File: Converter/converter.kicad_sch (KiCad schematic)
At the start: 30 parts, among them IC1 NCP5109ADR2G, IC2 NCP5109ADR2G

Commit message: assigned footprints for some passives
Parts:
- R_{small,bottom}1, R_{small,bottom}2, R_{small,top}1, R_{small,top}2: value R_small -> 0.75; footprint (none) -> Resistor_SMD:R_0603_1608Metric_Pad0.98x0.95mm_HandSolder
- TP1, TP2, TP3, TP4, TP5, TP6: footprint (none) -> TestPoint:TestPoint_Bridge_Pitch2.0mm_Drill0.7mm
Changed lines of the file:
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@@
 			)
 		)
-		(property "Footprint" ""
+		(property "Footprint" "TestPoint:TestPoint_Bridge_Pitch2.0mm_Drill0.7mm"
 			(at 147.32 118.11 0)
 			(effects
@@
 			)
 		)
-		(property "Value" "R_small"
+		(property "Value" "0.75"
 			(at 96.52 108.712 90)
 			(effects
@@
 			)
 		)
-		(property "Footprint" ""
+		(property "Footprint" "Resistor_SMD:R_0603_1608Metric_Pad0.98x0.95mm_HandSolder"
 			(at 96.774 105.664 90)
 			(effects
@@
 			)
 		)
-		(property "Value" "R_small"
+		(property "Value" "0.75"
 			(at 96.52 140.208 90)
 			(effects
@@
 			)
 		)
-		(property "Footprint" ""
+		(property "Footprint" "Resistor_SMD:R_0603_1608Metric_Pad0.98x0.95mm_HandSolder"
 			(at 96.774 136.144 90)
 			(effects
@@
 			)
 		)
-		(property "Value" "R_small"
+		(property "Value" "0.75"
 			(at 96.52 150.114 90)
 			(effects
@@
 			)
 		)
-		(property "Footprint" ""
+		(property "Footprint" "Resistor_SMD:R_0603_1608Metric_Pad0.98x0.95mm_HandSolder"
 			(at 96.774 146.304 90)
 			(effects
@@
 			)
 		)
-		(property "Footprint" ""
+		(property "Footprint" "TestPoint:TestPoint_Bridge_Pitch2.0mm_Drill0.7mm"
 			(at 172.72 118.11 0)
 			(effects
@@
 			)
 		)
-		(property "Footprint" ""
+		(property "Footprint" "TestPoint:TestPoint_Bridge_Pitch2.0mm_Drill0.7mm"
 			(at 147.32 107.95 0)
 			(effects
@@
 			)
 		)
-		(property "Footprint" ""
+		(property "Footprint" "TestPoint:TestPoint_Bridge_Pitch2.0mm_Drill0.7mm"
 			(at 172.72 107.95 0)
 			(effects
@@
 			)
 		)
-		(property "Value" "R_small"
+		(property "Value" "0.75"
 			(at 96.52 119.126 90)
 			(effects
@@
 			)
 		)
-		(property "Footprint" ""
+		(property "Footprint" "Resistor_SMD:R_0603_1608Metric_Pad0.98x0.95mm_HandSolder"
 			(at 96.774 115.824 90)
 			(effects
@@
 			)
 		)
-		(property "Footprint" ""
+		(property "Footprint" "TestPoint:TestPoint_Bridge_Pitch2.0mm_Drill0.7mm"
 			(at 172.72 97.79 0)
 			(effects
@@
 			)
 		)
-		(property "Footprint" ""
+		(property "Footprint" "TestPoint:TestPoint_Bridge_Pitch2.0mm_Drill0.7mm"
 			(at 147.32 97.79 0)
 			(effects

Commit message: more simulation work + fixed some things in root schematic
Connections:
- net +10V renamed +12V
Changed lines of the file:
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@@
 		)
 	)
-	(hierarchical_label "+10V"
+	(hierarchical_label "+12V"
 		(shape input)
 		(at 34.29 97.79 180)
@@
 		)
 	)
-	(hierarchical_label "+10V"
+	(hierarchical_label "+12V"
 		(shape input)
 		(at 34.29 128.27 180)

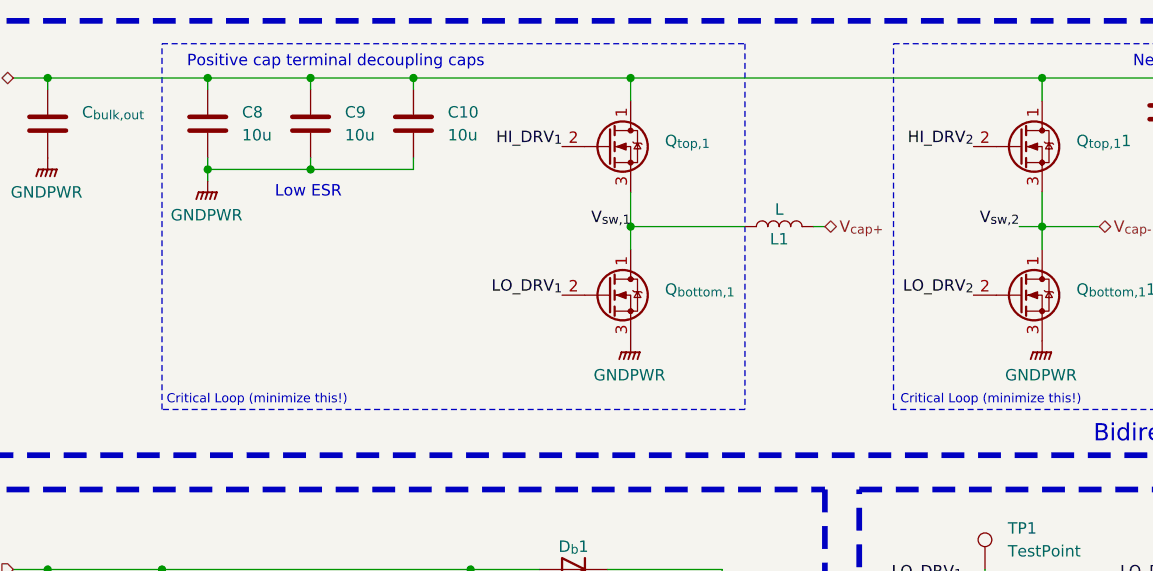
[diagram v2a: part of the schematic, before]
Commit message: fixed inductor connection
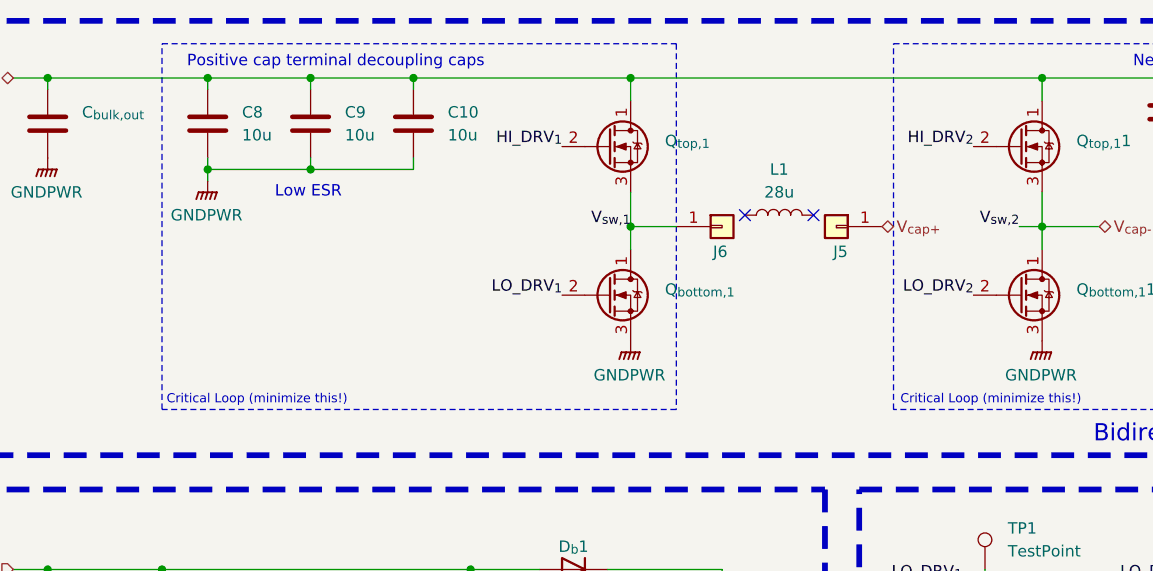
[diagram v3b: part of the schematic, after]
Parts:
- added J5, J6: Conn_01x01, NCP5109ADR2G:Inductor_wire_conn, symbol Connector_Generic:Conn_01x01
- L1: value L -> 28u
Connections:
- net V_{cap+}: now also J5.1 (Pin_1); no longer L1.2
- net V_{sw,1}: now also J6.1 (Pin_1); no longer L1.1
- no-connect marks 0 -> 2
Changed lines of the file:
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@@
 	(rectangle
 		(start 50.8 39.37)
-		(end 115.57 80.01)
+		(end 107.95 80.01)
 		(stroke
 			(width 0)
@@
 		(color 0 0 0 0)
 	)
+	(no_connect
+		(at 123.19 58.42)
+	)
+	(no_connect
+		(at 115.57 58.42)
+	)
 	(wire
 		(pts
@@
 	(wire
 		(pts
-			(xy 102.87 59.69) (xy 102.87 62.23)
-		)
-		(stroke
-			(width 0)
-			(type default)
-		)
-	)
-	(wire
-		(pts
 			(xy 85.09 106.68) (xy 85.09 97.79)
 		)
@@
 	(wire
 		(pts
+			(xy 102.87 59.69) (xy 107.95 59.69)
+		)
+		(stroke
+			(width 0)
+			(type default)
+		)
+	)
+	(wire
+		(pts
 			(xy 167.64 107.95) (xy 167.64 109.22)
 		)
@@
 	(wire
 		(pts
-			(xy 123.19 59.69) (xy 124.46 59.69)
+			(xy 55.88 43.18) (xy 67.31 43.18)
 		)
 		(stroke
@@
 	(wire
 		(pts
-			(xy 55.88 43.18) (xy 67.31 43.18)
+			(xy 162.56 52.07) (xy 173.99 52.07)
 		)
 		(stroke
@@
 	(wire
 		(pts
-			(xy 162.56 52.07) (xy 173.99 52.07)
+			(xy 102.87 59.69) (xy 102.87 62.23)
 		)
 		(stroke
@@
 	(wire
 		(pts
-			(xy 102.87 59.69) (xy 115.57 59.69)
-		)
-		(stroke
-			(width 0)
-			(type default)
-		)
-	)
-	(wire
-		(pts
 			(xy 173.99 43.18) (xy 185.42 43.18)
 		)
@@
 	(hierarchical_label "V_{cap+}"
 		(shape bidirectional)
-		(at 124.46 59.69 0)
+		(at 130.81 59.69 0)
 		(effects
 			(font
@@
 	)
 	(symbol
+		(lib_id "Connector_Generic:Conn_01x01")
+		(at 125.73 59.69 0)
+		(mirror y)
+		(unit 1)
+		(exclude_from_sim no)
+		(in_bom yes)
+		(on_board yes)
+		(dnp no)
+		(property "Reference" "J5"
+			(at 127 62.4839 0)
+			(effects
+				(font
+					(size 1.27 1.27)
+				)
+				(justify left)
+			)
+		)
+		(property "Value" "Conn_01x01"
+			(at 123.19 60.9599 0)
+			(effects
+				(font
+					(size 1.27 1.27)
+				)
+				(justify left)
+				(hide yes)
+			)
+		)
+		(property "Footprint" "NCP5109ADR2G:Inductor_wire_conn"
+			(at 125.73 59.69 0)
+			(effects
+				(font
+					(size 1.27 1.27)
+				)
+				(hide yes)
+			)
+		)
+		(property "Datasheet" "~"
+			(at 125.73 59.69 0)
+			(effects
+				(font
+					(size 1.27 1.27)
+				)
+				(hide yes)
+			)
+		)
+		(property "Description" "Generic connector, single row, 01x01, script generated (kicad-library-utils/schlib/autogen/connector/)"
+			(at 125.73 59.69 0)
+			(effects
+				(font
+					(size 1.27 1.27)
+				)
+				(hide yes)
+			)
+		)
+		(pin "1"
+		)
+		(instances
+			(project "Supercap"
+				(path "/98ee8313-37ab-4329-91ab-b5710476f82f/66de8ce3-68f9-4d35-858c-1420192a373c"
+					(reference "J5")
+					(unit 1)
+				)
+			)
+		)
+	)
+	(symbol
 		(lib_id "Transistor_FET:BSB013NE2LXI")
 		(at 100.33 67.31 0)
@@
 	)
 	(symbol
-		(lib_id "Device:L")
-		(at 119.38 59.69 90)
-		(unit 1)
-		(exclude_from_sim no)
-		(in_bom yes)
-		(on_board yes)
-		(dnp no)
-		(property "Reference" "L1"
-			(at 119.38 61.087 90)
-			(effects
-				(font
-					(size 1.27 1.27)
-				)
-			)
-		)
-		(property "Value" "L"
-			(at 119.38 57.785 90)
-			(effects
-				(font
-					(size 1.27 1.27)
-				)
-			)
-		)
-		(property "Footprint" ""
-			(at 119.38 59.69 0)
-			(effects
-				(font
-					(size 1.27 1.27)
-				)
-				(hide yes)
-			)
-		)
-		(property "Datasheet" "~"
-			(at 119.38 59.69 0)
-			(effects
-				(font
-					(size 1.27 1.27)
-				)
-				(hide yes)
-			)
-		)
-		(property "Description" ""
-			(at 119.38 59.69 0)
-			(effects
-				(font
-					(size 1.27 1.27)
-				)
-				(hide yes)
-			)
-		)
-		(pin "1"
-		)
-		(pin "2"
-		)
-		(instances
-			(project "Supercap"
-				(path "/98ee8313-37ab-4329-91ab-b5710476f82f/66de8ce3-68f9-4d35-858c-1420192a373c"
-					(reference "L1")
-					(unit 1)
-				)
-			)
-		)
-	)
-	(symbol
 		(lib_id "Connector:TestPoint")
 		(at 142.24 118.11 0)
@@
 	)
 	(symbol
+		(lib_id "Device:L")
+		(at 119.38 58.42 90)
+		(unit 1)
+		(exclude_from_sim no)
+		(in_bom yes)
+		(on_board no)
+		(dnp no)
+		(fields_autoplaced yes)
+		(property "Reference" "L1"
+			(at 119.38 53.34 90)
+			(effects
+				(font
+					(size 1.27 1.27)
+				)
+			)
+		)
+		(property "Value" "28u"
+			(at 119.38 55.88 90)
+			(effects
+				(font
+					(size 1.27 1.27)
+				)
+			)
+		)
+		(property "Footprint" ""
+			(at 119.38 58.42 0)
+			(effects
+				(font
+					(size 1.27 1.27)
+				)
+				(hide yes)
+			)
+		)
+		(property "Datasheet" "~"
+			(at 119.38 58.42 0)
+			(effects
+				(font
+					(size 1.27 1.27)
+				)
+				(hide yes)
+			)
+		)
+		(property "Description" "Inductor"
+			(at 119.38 58.42 0)
+			(effects
+				(font
+					(size 1.27 1.27)
+				)
+				(hide yes)
+			)
+		)
+		(pin "1"
+		)
+		(pin "2"
+		)
+		(instances
+			(project "Supercap"
+				(path "/98ee8313-37ab-4329-91ab-b5710476f82f/66de8ce3-68f9-4d35-858c-1420192a373c"
+					(reference "L1")
+					(unit 1)
+				)
+			)
+		)
+	)
+	(symbol
 		(lib_id "Device:R_US")
 		(at 96.52 106.68 90)
@@
 					(unit 1)
 				)
+			)
+		)
+	)
+	(symbol
+		(lib_id "Connector_Generic:Conn_01x01")
+		(at 113.03 59.69 0)
+		(unit 1)
+		(exclude_from_sim no)
+		(in_bom yes)
+		(on_board yes)
+		(dnp no)
+		(property "Reference" "J6"
+			(at 112.014 62.4839 0)
+			(effects
+				(font
+					(size 1.27 1.27)
+				)
+				(justify left)
+			)
+		)
+		(property "Value" "Conn_01x01"
+			(at 115.57 60.9599 0)
+			(effects
+				(font
+					(size 1.27 1.27)
+				)
+				(justify left)
+				(hide yes)
+			)
+		)
+		(property "Footprint" "NCP5109ADR2G:Inductor_wire_conn"
+			(at 113.03 59.69 0)
+			(effects
+				(font
+					(size 1.27 1.27)
+				)
+				(hide yes)
+			)
+		)
+		(property "Datasheet" "~"
+			(at 113.03 59.69 0)
+			(effects
+				(font
+					(size 1.27 1.27)
+				)
+				(hide yes)
+			)
+		)
+		(property "Description" "Generic connector, single row, 01x01, script generated (kicad-library-utils/schlib/autogen/connector/)"
+			(at 113.03 59.69 0)
+			(effects
+				(font
+					(size 1.27 1.27)
+				)
+				(hide yes)
+			)
+		)
+		(pin "1"
+		)
+		(instances
+			(project "Supercap"
+				(path "/98ee8313-37ab-4329-91ab-b5710476f82f/66de8ce3-68f9-4d35-858c-1420192a373c"
+					(reference "J6")
+					(unit 1)
+				)

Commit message: decoupling capacitors assigned
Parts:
- C10, C8, C9: footprint (none) -> Capacitor_SMD:C_0201_0603Metric; Mouser Part Number (none) -> 81-ZRB18AR6YA106ME1L
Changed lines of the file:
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@@
 			)
 		)
-		(property "Footprint" ""
+		(property "Footprint" "Capacitor_SMD:C_0201_0603Metric"
 			(at 79.7052 52.07 0)
 			(effects
@@
 			)
 		)
-		(property "Datasheet" ""
+		(property "Datasheet" "https://pim.murata.com/asset/pim4/ceramicCapacitorSMD/ZRB18AR6YA106ME01-02A-EN_PDF_CERAMICCAPACITORSMD"
 			(at 78.74 48.26 0)
 			(effects
@@
 			)
 		)
-		(property "Mouser Part Number" ""
+		(property "Mouser Part Number" "81-ZRB18AR6YA106ME1L"
 			(at 78.74 48.26 0)
 			(effects
@@
 			)
 		)
-		(property "Footprint" ""
+		(property "Footprint" "Capacitor_SMD:C_0201_0603Metric"
 			(at 56.8452 52.07 0)
 			(effects
@@
 			)
 		)
-		(property "Datasheet" ""
+		(property "Datasheet" "https://pim.murata.com/asset/pim4/ceramicCapacitorSMD/ZRB18AR6YA106ME01-02A-EN_PDF_CERAMICCAPACITORSMD"
 			(at 55.88 48.26 0)
 			(effects
@@
 			)
 		)
-		(property "Mouser Part Number" ""
+		(property "Mouser Part Number" "81-ZRB18AR6YA106ME1L"
 			(at 55.88 48.26 0)
 			(effects
@@
 			)
 		)
-		(property "Footprint" ""
+		(property "Footprint" "Capacitor_SMD:C_0201_0603Metric"
 			(at 68.2752 52.07 0)
 			(effects
@@
 			)
 		)
-		(property "Datasheet" ""
+		(property "Datasheet" "https://pim.murata.com/asset/pim4/ceramicCapacitorSMD/ZRB18AR6YA106ME01-02A-EN_PDF_CERAMICCAPACITORSMD"
 			(at 67.31 48.26 0)
 			(effects
@@
 			)
 		)
-		(property "Mouser Part Number" ""
+		(property "Mouser Part Number" "81-ZRB18AR6YA106ME1L"
 			(at 67.31 48.26 0)
 			(effects

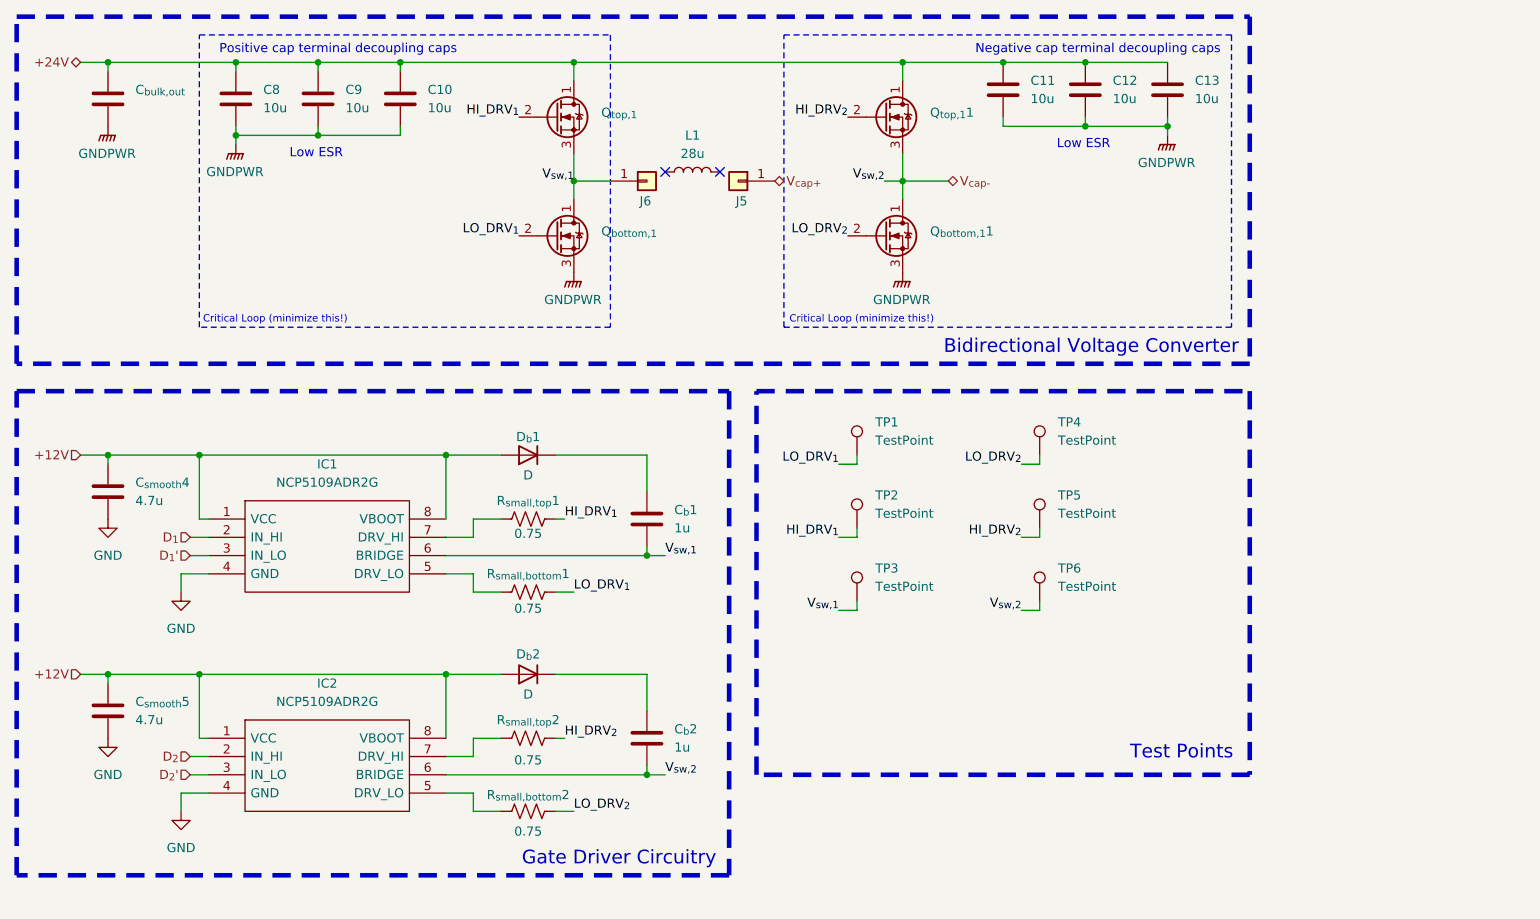
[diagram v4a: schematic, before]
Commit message: removed v1 files and assigned mouser part numbers
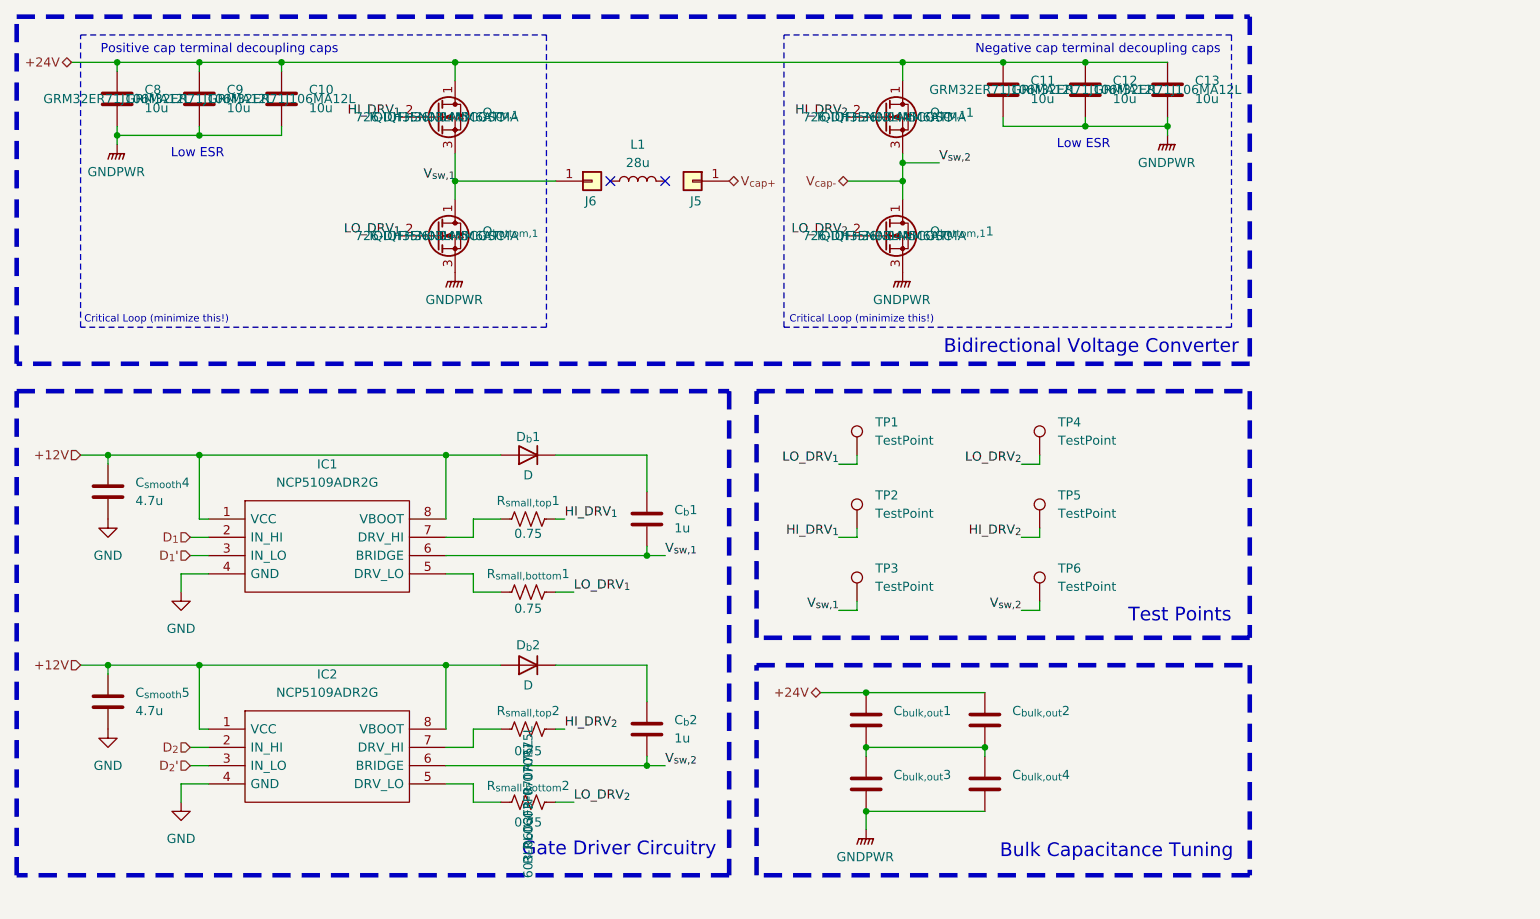
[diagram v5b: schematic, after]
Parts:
- removed C_{bulk,out}: ~, symbol Device:C
- added C_{bulk,out}1, C_{bulk,out}2, C_{bulk,out}3, C_{bulk,out}4: ~, Capacitor_SMD:C_0603_1608Metric_Pad1.08x0.95mm_HandSolder, symbol Device:C
- C10, C8, C9: footprint Capacitor_SMD:C_0201_0603Metric -> Capacitor_SMD:C_1210_3225Metric_Pad1.33x2.70mm_HandSolder; Manufacturer_Part_Number (none) -> GRM32ER71J106MA12L; Mouser Part Number 81-ZRB18AR6YA106ME1L -> 81-GRM32ER71J106MA2L
- C11, C12, C13: footprint (none) -> Capacitor_SMD:C_1210_3225Metric_Pad1.33x2.70mm_HandSolder; Manufacturer_Part_Number (none) -> GRM32ER71J106MA12L; Mouser Part Number (none) -> 81-GRM32ER71J106MA2L
- Q_{bottom,1}, Q_{bottom,1}1, Q_{top,1}, Q_{top,1}1: Manufacturer_Part_Number (none) -> IQDH35N03LM5CGSC; Mouser Part Number (none) -> 726-IQFH36N04NM6ATMA
- R_{small,bottom}1, R_{small,bottom}2, R_{small,top}1, R_{small,top}2: Manufacturer_Part_Number (none) -> RL0603FR-070R75L; Mouser Part Number (none) -> 603-RL0603FR-070R75L
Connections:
- net +24V: now also C_{bulk,out}1.1, C_{bulk,out}2.1
- net GNDPWR: now also C_{bulk,out}3.2, C_{bulk,out}4.2
- new net: C_{bulk,out}1.2, C_{bulk,out}2.2, C_{bulk,out}3.1, C_{bulk,out}4.1
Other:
- note added: "Bulk Capacitance Tuning"
- moved on the sheet: C10, C8, C9, C_{b}2, C_{smooth}5, D_{b}2, IC2, J5, J6, L1, Q_{bottom,1}, Q_{top,1}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

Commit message: began layout
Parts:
- J1: renamed from J6; footprint NCP5109ADR2G:Inductor_wire_conn -> Robomaster_Passives:Inductor_wire_conn
- J2: renamed from J5; footprint NCP5109ADR2G:Inductor_wire_conn -> Robomaster_Passives:Inductor_wire_conn
- Q_{bottom,1}1: renamed from Q_{bottom,1}; footprint IQDH35N03LM5CGSCATMA1_MOSFET:IQDH45N04LM6CGSCATMA1 -> Robomaster_ICs:IQDH45N04LM6CGSCATMA1
- Q_{bottom,1}2: renamed from Q_{bottom,1}1; footprint IQDH35N03LM5CGSCATMA1_MOSFET:IQDH45N04LM6CGSCATMA1 -> Robomaster_ICs:IQDH45N04LM6CGSCATMA1
- Q_{top,1}1: renamed from Q_{top,1}; footprint IQDH35N03LM5CGSCATMA1_MOSFET:IQDH45N04LM6CGSCATMA1 -> Robomaster_ICs:IQDH45N04LM6CGSCATMA1
- Q_{top,1}2: renamed from Q_{top,1}1; footprint IQDH35N03LM5CGSCATMA1_MOSFET:IQDH45N04LM6CGSCATMA1 -> Robomaster_ICs:IQDH45N04LM6CGSCATMA1
- renumbered C_{bulk,out}3 to C_{bulk,out}2, C_{bulk,out}2 to C_{bulk,out}3, C8 to C_{d1}1, C9 to C_{d2}1, C10 to C_{d3}1, C11 to C_{d4}1, C12 to C_{d5}1, C13 to C_{d6}1, C_{smooth}4 to C_{smooth}5, C_{smooth}5 to C_{smooth}6
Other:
- moved on the sheet: J1, L1

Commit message: mostly done with first order layout
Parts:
- C_{d1}1, C_{d2}1, C_{d3}1, C_{d4}1, C_{d5}1, C_{d6}1: Manufacturer_Part_Number GRM32ER71J106MA12L -> CL32B106KMVNNWE; Mouser Part Number 81-GRM32ER71J106MA2L -> 187-CL32B106KMVNNWE
- renumbered C_{smooth}5 to C_{smooth}6, C_{smooth}6 to C_{smooth}7
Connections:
- net GND is gone; now on net GNDPWR: C_{smooth}6.2, C_{smooth}7.2, IC1.4 (GND), IC2.4 (GND)
- net +12V: no longer IC1.8 (VBOOT), IC2.8 (VBOOT)
- net C_TUNE_MID: now reaches C_{bulk,out}1.2, C_{bulk,out}2.1, C_{bulk,out}3.2, C_{bulk,out}4.1
- net HI_{R1}: now reaches IC1.7 (DRV_HI), R_{small,top}1.1
- net V_{boot}2: now reaches C_{b}2.1, D_{b}2.1 (K)
- net V_{boot}2: now also IC2.8 (VBOOT)
- net V_{boot}1: now reaches C_{b}1.1, D_{b}1.1 (K)
- net V_{boot}1: now also IC1.8 (VBOOT)
- net HI_{R2}: now reaches IC2.7 (DRV_HI), R_{small,top}2.1
- net LO_{R2}: now reaches IC2.5 (DRV_LO), R_{small,bottom}2.1
- net LO_{R1}: now reaches IC1.5 (DRV_LO), R_{small,bottom}1.1
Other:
- company: (none) -> UT Robomaster
- title: (none) -> DC/DC Converter and Gate Driver Board
- moved on the sheet: C_{bulk,out}1, C_{bulk,out}2, C_{bulk,out}3, C_{bulk,out}4, C_{b}1, C_{b}2, C_{d1}1, C_{d2}1, C_{d3}1, C_{d4}1, C_{d5}1, C_{d6}1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
